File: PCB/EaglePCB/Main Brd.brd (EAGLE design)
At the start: 106.7 x 102.9 mm, 65 parts, among them J2 702461401, U1 ATWINC1500-MR210PB1952-T, U3 MSP430FR2355TDBTRDBT0038A_M, U6 ARJM11C7-114-BA-EW2

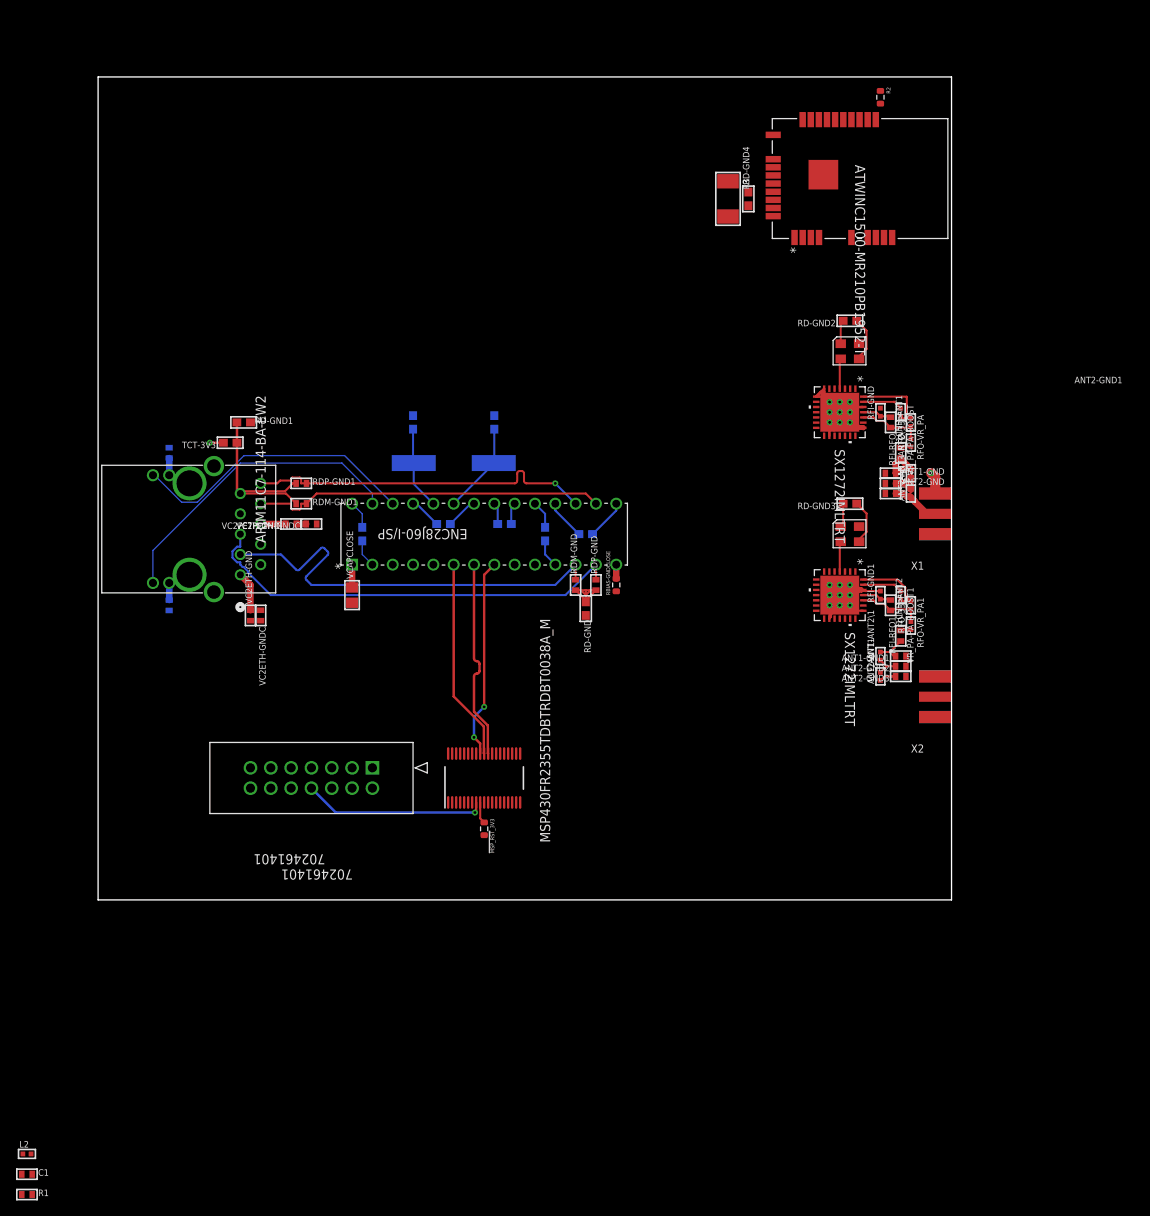
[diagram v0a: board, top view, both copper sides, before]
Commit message: more traces ran, ENC, JTAG
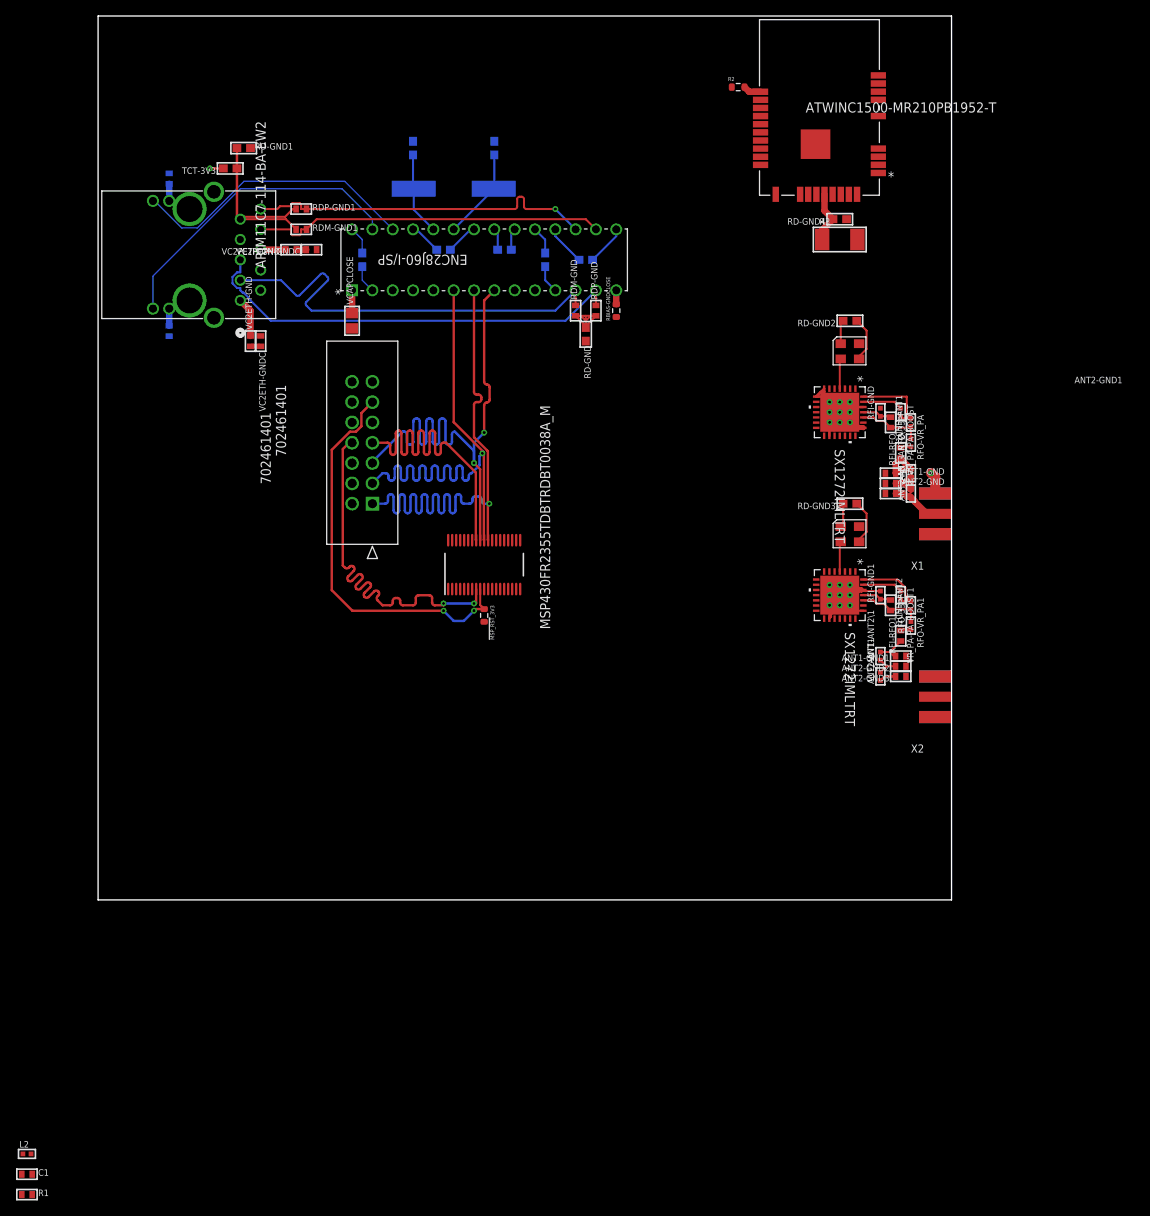
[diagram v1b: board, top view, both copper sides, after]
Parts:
- moved ETH 34.3 mm to (31.8, 76.2)
- moved LEDG 34.3 mm to (8.89, 71.1)
- moved OSC1-GND 34.3 mm to (49.5, 94.0)
- moved OSC2-GND 34.3 mm to (39.4, 94.0)
- moved RD-GND 34.3 mm to (61.0, 70.7)
- moved RD-GND1 34.3 mm to (18.2, 94.0)
- moved U$2 34.3 mm to (44.5, 88.9)
- moved U6 34.3 mm to (17.8, 74.9)
- moved VSS-VDD_ETH 34.3 mm to (33.0, 80.0)
- moved VSSRX-VDDRX 34.3 mm to (55.9, 80.0)
- moved VSSTX-VDDTX 34.3 mm to (61.0, 80.0)
- moved LEDY 34.3 mm to (8.89, 90.2)
- moved RBIAS-GNDCLOSE 34.3 mm to (64.8, 73.7)
- moved RDM-GND 34.3 mm to (59.7, 73.7)
- moved RDP-GND 34.3 mm to (62.2, 73.7)
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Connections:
- removed net A0_CLK: J2.5
- removed net A0_MISO: J2.3
- removed net A0_MOSI: J2.1
- removed net ETH_SCK: ETH.8, U3.30
- new net ETH_CLK: ETH.8, J2.5, U3.30
- net ETH_MISO: now also J2.3
- net ETH_MOSI: now also J2.1
- net GND: now also U6.15, U6.16
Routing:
- net ETH_CLK: track 0.00 -> 69.7 mm, vias 0 -> 2
- net ETH_MOSI: track 24.9 -> 74.0 mm, vias 0 -> 1
- net !MSP_RST: track 2.71 -> 50.2 mm, vias 0 -> 2
- net MSP_TCK: track 0.00 -> 46.2 mm
- net ETH_MISO: track 25.2 -> 67.6 mm, vias 0 -> 1
- net MSP_TEST: track 23.0 -> 48.2 mm, vias 1 -> 2
- net ETH_SCK: track 25.0 -> 0.00 mm, vias 2 -> 0
- net N$13: track 0.00 -> 6.65 mm
- net ATC_SPI_CFG: track 0.00 -> 2.24 mm
- net N$5: track 0.00 -> 1.27 mm
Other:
- board size 106.7 x 102.9 mm -> 106.7 x 110.5 mm

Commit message: pcb moving forward
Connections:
- net LORA1_TX renamed LORA1_RX
- net LORA2_RX renamed LORA2_TX
- removed net A1_CLK: U3.22
- removed net A1_MISO: U3.21
- removed net A1_MOSI: U3.20
- removed net ATC_SSN: U1.16
- removed net B0_CLK: U3.6
- removed net B0_MISO: U3.5
- removed net B0_MOSI: U3.4
- removed net B1_CLK: U3.18
- removed net B1_MISO: U3.17
- removed net B1_MOSI: U3.16
- removed net MSP_TCK: J2.7, U3.31
- removed net N$21: U3.23
- removed net SPI_SCK: U1.18
- new net ATC_CHIPSEL: U1.16, U3.23
- new net ATC_SCK: U1.18, U3.22
- net !ATC_IRQ: now also U3.35
- net !ATC_RST: now also U3.1
- net !ETH_CHIPSEL: now also J2.7, U3.31
- net !ETH_IRQ: now also U3.26
- net !ETH_RST: now also U3.27
- net ATC_MISO: now also U3.21
- net ATC_MOSI: now also U3.20
- net LORA1_CHIPSEL: now also U3.19
- net LORA1_IRQ: now also U3.2
- net LORA1_MISO: now also U3.16
- net LORA1_MOSI: now also U3.17
- net LORA1_RST: now also U3.3
- net LORA1_SCK: now also U3.18
- net LORA2_CHIPSEL: now also U3.7
- net LORA2_IRQ: now also U3.15
- net LORA2_MISO: now also U3.4
- net LORA2_MOSI: now also U3.5
- net LORA2_RST: now also U3.25
- net LORA2_SCK: now also U3.6
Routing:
- net !ATC_IRQ: track 0.00 -> 71.0 mm, vias 0 -> 4
- net LORA1_RST: track 0.00 -> 66.6 mm, vias 0 -> 2
- net LORA1_IRQ: track 0.00 -> 65.2 mm, vias 0 -> 2
- net ATC_CHIPSEL: track 0.00 -> 63.5 mm
- net ATC_MISO: track 0.00 -> 62.0 mm
- net LORA2_MOSI: track 0.00 -> 59.9 mm, vias 0 -> 2
- net ATC_MOSI: track 0.00 -> 59.8 mm, vias 0 -> 1
- net LORA2_MISO: track 0.00 -> 57.7 mm
- net ATC_SCK: track 0.00 -> 56.3 mm
- net LORA2_CHIPSEL: track 0.00 -> 56.0 mm, vias 0 -> 2
- net LORA2_SCK: track 0.00 -> 54.2 mm
- net LORA1_MISO: track 0.00 -> 53.7 mm
- net LORA1_MOSI: track 0.00 -> 52.2 mm
- net LORA1_SCK: track 0.00 -> 50.7 mm
- net LORA1_CHIPSEL: track 0.00 -> 50.4 mm, vias 0 -> 2
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
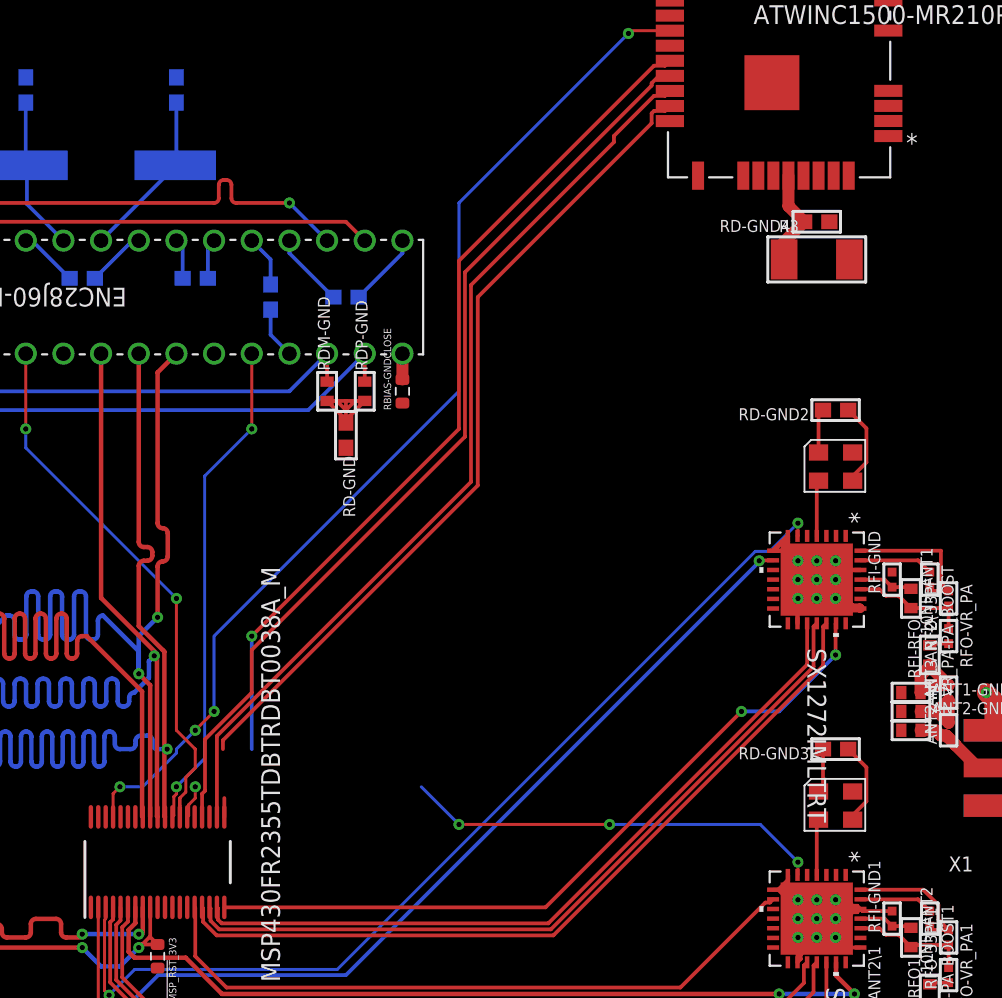
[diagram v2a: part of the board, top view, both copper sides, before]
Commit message: all SPi traced
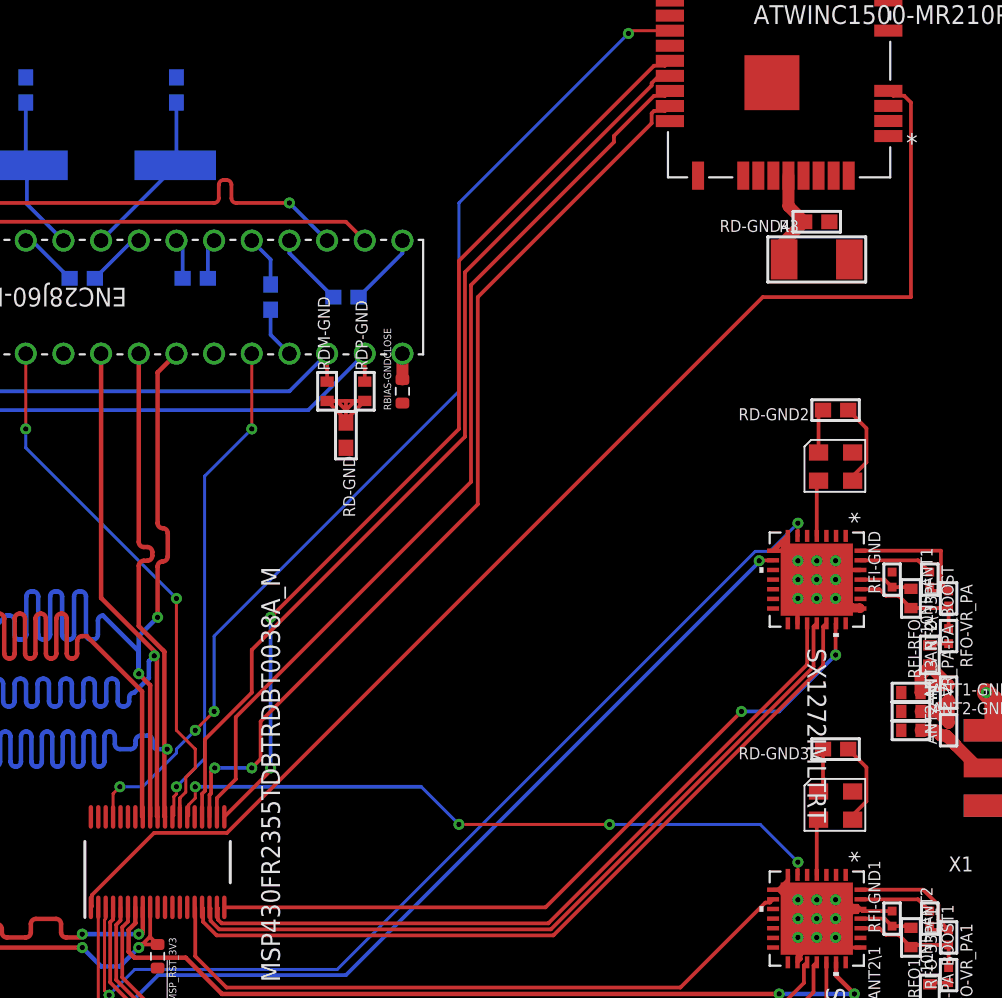
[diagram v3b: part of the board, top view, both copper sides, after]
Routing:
- net !ATC_RST: track 0.00 -> 87.8 mm
- net LORA2_RST: track 30.6 -> 45.9 mm
- net ATC_SCK: track 56.3 -> 62.7 mm, vias 0 -> 2
- net ATC_MOSI: track 59.8 -> 63.9 mm, vias 1 -> 2
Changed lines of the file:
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@@
 <wire x1="91.44" y1="41.91" x2="91.44" y2="41.0764" width="0.2032" layer="1"/>
 <wire x1="91.44" y1="41.0764" x2="91.41" y2="41.0464" width="0.2032" layer="1"/>
-<wire x1="50.8" y1="46.99" x2="66.04" y2="46.99" width="0" layer="19" extent="16-16"/>
+<wire x1="50.8" y1="46.99" x2="66.04" y2="46.99" width="0.254" layer="16"/>
 </signal>
 <signal name="LORA2_IRQ">
@@
 <contactref element="U1" pad="4"/>
 <contactref element="U3" pad="1"/>
-<wire x1="43.76" y1="38.86" x2="97.535003125" y2="93.918" width="0" layer="19" extent="1-1"/>
+<wire x1="43.76" y1="38.86" x2="43.830596875" y2="38.930596875" width="0.254" layer="1"/>
+<wire x1="43.830596875" y1="38.930596875" x2="43.830596875" y2="39.687859375" width="0.254" layer="1"/>
+<wire x1="43.830596875" y1="39.687859375" x2="48.0233375" y2="43.8806" width="0.254" layer="1"/>
+<wire x1="48.0233375" y1="43.8806" x2="52.9378625" y2="43.8806" width="0.254" layer="1"/>
+<wire x1="89.0672625" y1="80.01" x2="99.06" y2="80.01" width="0.254" layer="1"/>
+<wire x1="52.9378625" y1="43.8806" x2="89.0672625" y2="80.01" width="0.254" layer="1"/>
+<wire x1="98.603234375" y1="93.587796875" x2="97.86520625" y2="93.587796875" width="0.254" layer="1"/>
+<wire x1="97.86520625" y1="93.587796875" x2="97.535003125" y2="93.918" width="0.254" layer="1"/>
+<wire x1="99.06" y1="80.01" x2="99.06" y2="93.13103125" width="0.254" layer="1"/>
+<wire x1="99.06" y1="93.13103125" x2="98.603234375" y2="93.587796875" width="0.254" layer="1"/>
 </signal>
 <signal name="!ATC_IRQ">
@@
 <wire x1="81.736765625" y1="93.581796875" x2="79.033096875" y2="90.878128125" width="0.254" layer="1"/>
 <wire x1="79.033096875" y1="90.878128125" x2="79.033096875" y2="90.463096875" width="0.254" layer="1"/>
-<wire x1="52.26" y1="50.4152625" x2="52.26" y2="44.96" width="0.254" layer="1"/>
+<wire x1="53.53" y1="51.6852625" x2="53.53" y2="47.5" width="0.254" layer="1"/>
+<wire x1="53.53" y1="47.5" x2="52.26" y2="46.23" width="0.254" layer="1"/>
+<wire x1="52.26" y1="46.23" x2="52.26" y2="44.96" width="0.254" layer="1"/>
 <wire x1="79.033096875" y1="90.463096875" x2="69.3928" y2="80.8228" width="0.254" layer="1"/>
 <wire x1="69.3928" y1="80.8228" x2="69.3928" y2="67.5480625" width="0.254" layer="1"/>
-<wire x1="69.3928" y1="67.5480625" x2="52.26" y2="50.4152625" width="0.254" layer="1"/>
+<wire x1="69.3928" y1="67.5480625" x2="53.53" y2="51.6852625" width="0.254" layer="1"/>
 </signal>
 <signal name="ATC_SCK">
@@
 <wire x1="81.573096875" y1="92.402128125" x2="81.573096875" y2="91.733096875" width="0.254" layer="1"/>
 <wire x1="81.573096875" y1="91.733096875" x2="69.85" y2="80.01" width="0.254" layer="1"/>
-<wire x1="69.85" y1="80.01" x2="69.85" y2="67.31" width="0.254" layer="1"/>
-<wire x1="69.85" y1="67.31" x2="52.6664" y2="50.1264" width="0.254" layer="1"/>
-<wire x1="52.6664" y1="50.1264" x2="52.6664" y2="49.53" width="0.254" layer="1"/>
-<wire x1="52.6664" y1="49.53" x2="51.759996875" y2="44.96" width="0" layer="19" extent="1-1"/>
+<wire x1="69.85" y1="80.01" x2="69.85" y2="66.04" width="0.254" layer="1"/>
+<wire x1="69.85" y1="66.04" x2="55.2064" y2="51.3964" width="0.254" layer="1"/>
+<via x="52.1152" y="48.26" extent="1-16" drill="0.35"/>
+<wire x1="51.759996875" y1="44.96" x2="51.759996875" y2="46.445271875" width="0.254" layer="1"/>
+<wire x1="51.759996875" y1="46.445271875" x2="51.864" y2="46.549275" width="0.254" layer="1"/>
+<wire x1="51.864" y1="46.549275" x2="51.864" y2="48.0088" width="0.254" layer="1"/>
+<wire x1="51.864" y1="48.0088" x2="52.1152" y2="48.26" width="0.254" layer="1"/>
+<wire x1="52.1152" y1="48.26" x2="54.61" y2="48.26" width="0.254" layer="16"/>
+<via x="54.61" y="48.26" extent="1-16" drill="0.35"/>
+<wire x1="54.61" y1="48.26" x2="55.2064" y2="48.8564" width="0.254" layer="1"/>
+<wire x1="55.2064" y1="51.3964" x2="55.2064" y2="48.8564" width="0.254" layer="1"/>
 </signal>
 <signal name="ATC_MOSI">
@@
 <wire x1="81.736765625" y1="95.613796875" x2="68.58" y2="82.45703125" width="0.254" layer="1"/>
 <wire x1="68.58" y1="82.45703125" x2="68.58" y2="71.12" width="0.254" layer="1"/>
-<wire x1="68.58" y1="71.12" x2="54.61" y2="57.15" width="0.254" layer="1"/>
-<via x="54.61" y="57.15" extent="1-16" drill="0.35"/>
-<wire x1="54.61" y1="57.15" x2="54.61" y2="49.53" width="0.254" layer="16"/>
-<wire x1="52.76" y1="46.23" x2="52.76" y2="44.96" width="0.254" layer="1"/>
-<wire x1="52.76" y1="46.23" x2="54.61" y2="49.53" width="0" layer="19" extent="1-16"/>
+<wire x1="68.58" y1="71.12" x2="55.88" y2="58.42" width="0.254" layer="1"/>
+<via x="55.88" y="58.42" extent="1-16" drill="0.35"/>
+<wire x1="55.88" y1="58.42" x2="55.88" y2="48.26" width="0.254" layer="16"/>
+<wire x1="52.76" y1="44.96" x2="55.88" y2="48.08" width="0.254" layer="1"/>
+<wire x1="55.88" y1="48.08" x2="55.88" y2="48.26" width="0.254" layer="1"/>
+<via x="55.88" y="48.26" extent="1-16" drill="0.35"/>
 </signal>
 <signal name="ATC_SPI_CFG">
